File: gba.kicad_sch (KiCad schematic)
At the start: 16 parts, among them IC1 STM32MP157AAB3, IC7 S40FC004C1B2C00000, SW1 SW_MEC_5G, SW2 SW_MEC_5G

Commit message: added some part footprints
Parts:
- C1, C2: footprint (none) -> Capacitor_SMD:C_0603_1608Metric; MFN (none) -> 77-VJ0603Y103MXAPBC
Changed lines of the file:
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@@
       (effects (font (size 1.27 1.27)) (justify left))
     )
-    (property "Footprint" "" (at 232.41 40.64 0)
+    (property "Footprint" "Capacitor_SMD:C_0603_1608Metric" (at 232.41 40.64 0)
       (effects (font (size 1.27 1.27)) hide)
     )
@@
       (effects (font (size 1.27 1.27)) hide)
     )
-    (property "MFN" "" (at 232.41 40.64 0)
+    (property "MFN" " 77-VJ0603Y103MXAPBC " (at 232.41 40.64 0)
       (effects (font (size 1.27 1.27)) hide)
     )
@@
       (effects (font (size 1.27 1.27)) (justify left))
     )
-    (property "Footprint" "" (at 256.54 40.64 0)
+    (property "Footprint" "Capacitor_SMD:C_0603_1608Metric" (at 256.54 40.64 0)
       (effects (font (size 1.27 1.27)) hide)
     )
@@
       (effects (font (size 1.27 1.27)) hide)
     )
-    (property "MFN" "" (at 256.54 40.64 0)
+    (property "MFN" " 77-VJ0603Y103MXAPBC " (at 256.54 40.64 0)
       (effects (font (size 1.27 1.27)) hide)
     )

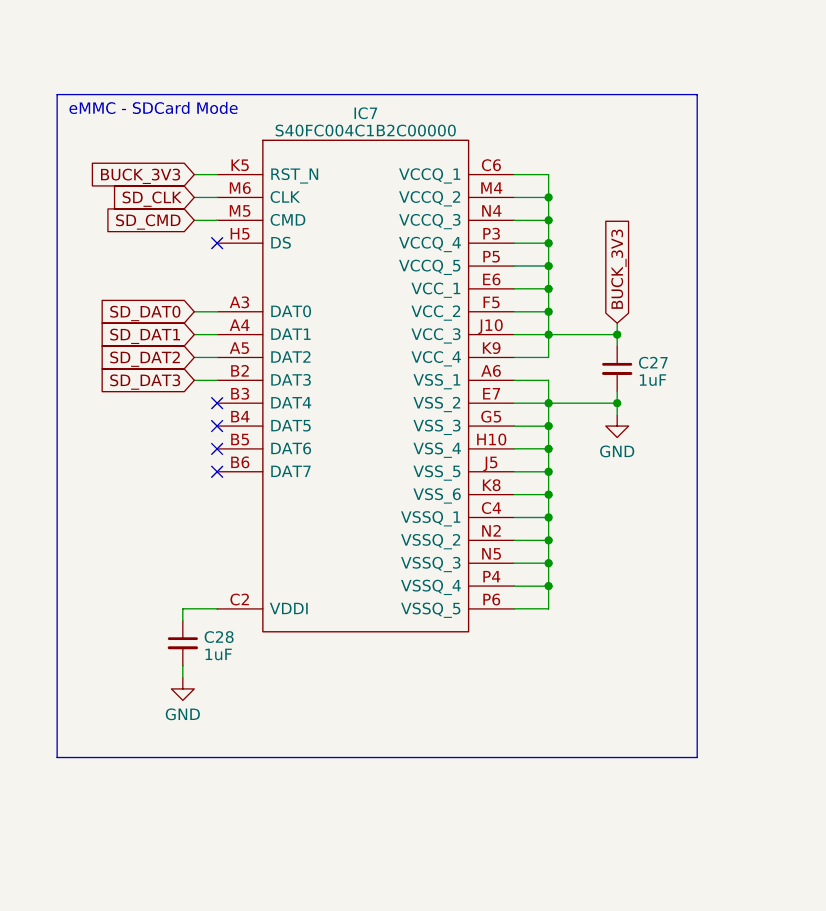
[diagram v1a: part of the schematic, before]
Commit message: Add Labels for DDR & DDR Power
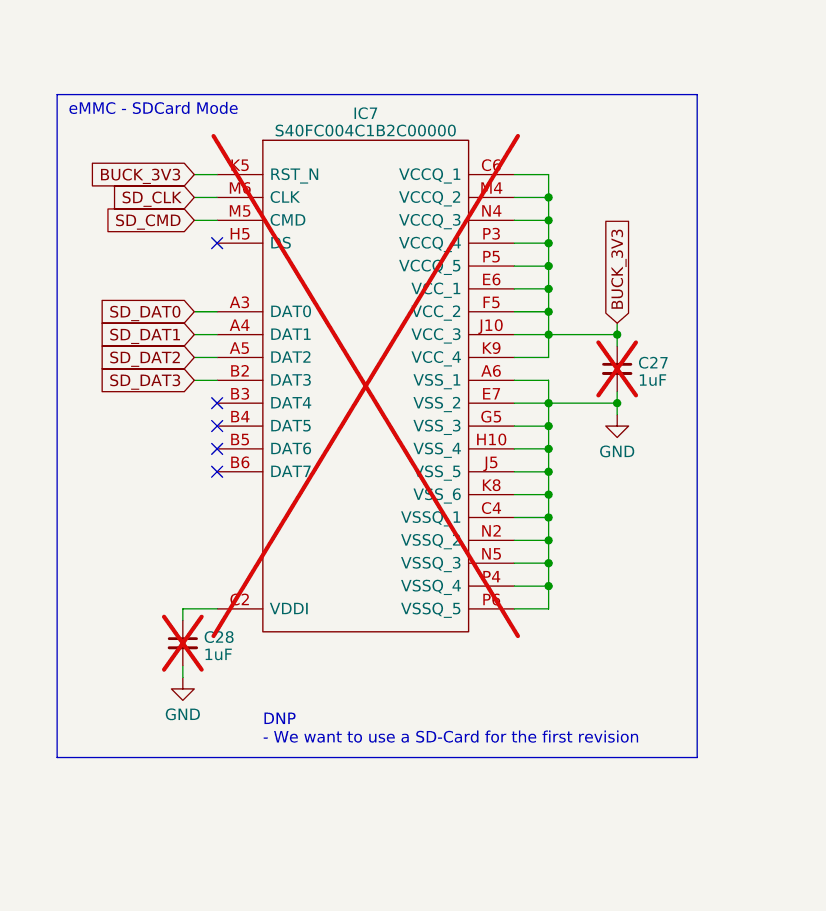
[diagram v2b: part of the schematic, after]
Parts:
- C27, C28, IC7: now not fitted
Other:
- note added: "DNP - We want to use a SD-Card for the first revision"
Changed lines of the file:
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@@
+    (effects (font (size 1.27 1.27)) (justify left bottom))
+  )
+  (text "DNP\n- We want to use a SD-Card for the first revision"
+    (at 353.06 97.79 0)
     (effects (font (size 1.27 1.27)) (justify left bottom))
   )
@@
   )
   (symbol (lib_id "Device:C_Small") (at 344.17 86.36 0) (unit 1)
-    (in_bom yes) (on_board yes) (dnp no) (fields_autoplaced)
+    (in_bom yes) (on_board yes) (dnp yes) (fields_autoplaced)
     (property "Reference" "C28" (at 346.4941 85.7226 0)
       (effects (font (size 1.27 1.27)) (justify left))
@@
   )
   (symbol (lib_id "Device:C_Small") (at 392.43 55.88 0) (unit 1)
-    (in_bom yes) (on_board yes) (dnp no) (fields_autoplaced)
+    (in_bom yes) (on_board yes) (dnp yes) (fields_autoplaced)
     (property "Reference" "C27" (at 394.7541 55.2426 0)
       (effects (font (size 1.27 1.27)) (justify left))
@@
   )
   (symbol (lib_id "ARMband:S40FC004C1B2C00000") (at 384.81 34.29 0) (unit 1)
-    (in_bom yes) (on_board yes) (dnp no) (fields_autoplaced)
+    (in_bom yes) (on_board yes) (dnp yes) (fields_autoplaced)
     (property "Reference" "IC7" (at 364.49 27.5209 0)
       (effects (font (size 1.27 1.27)))

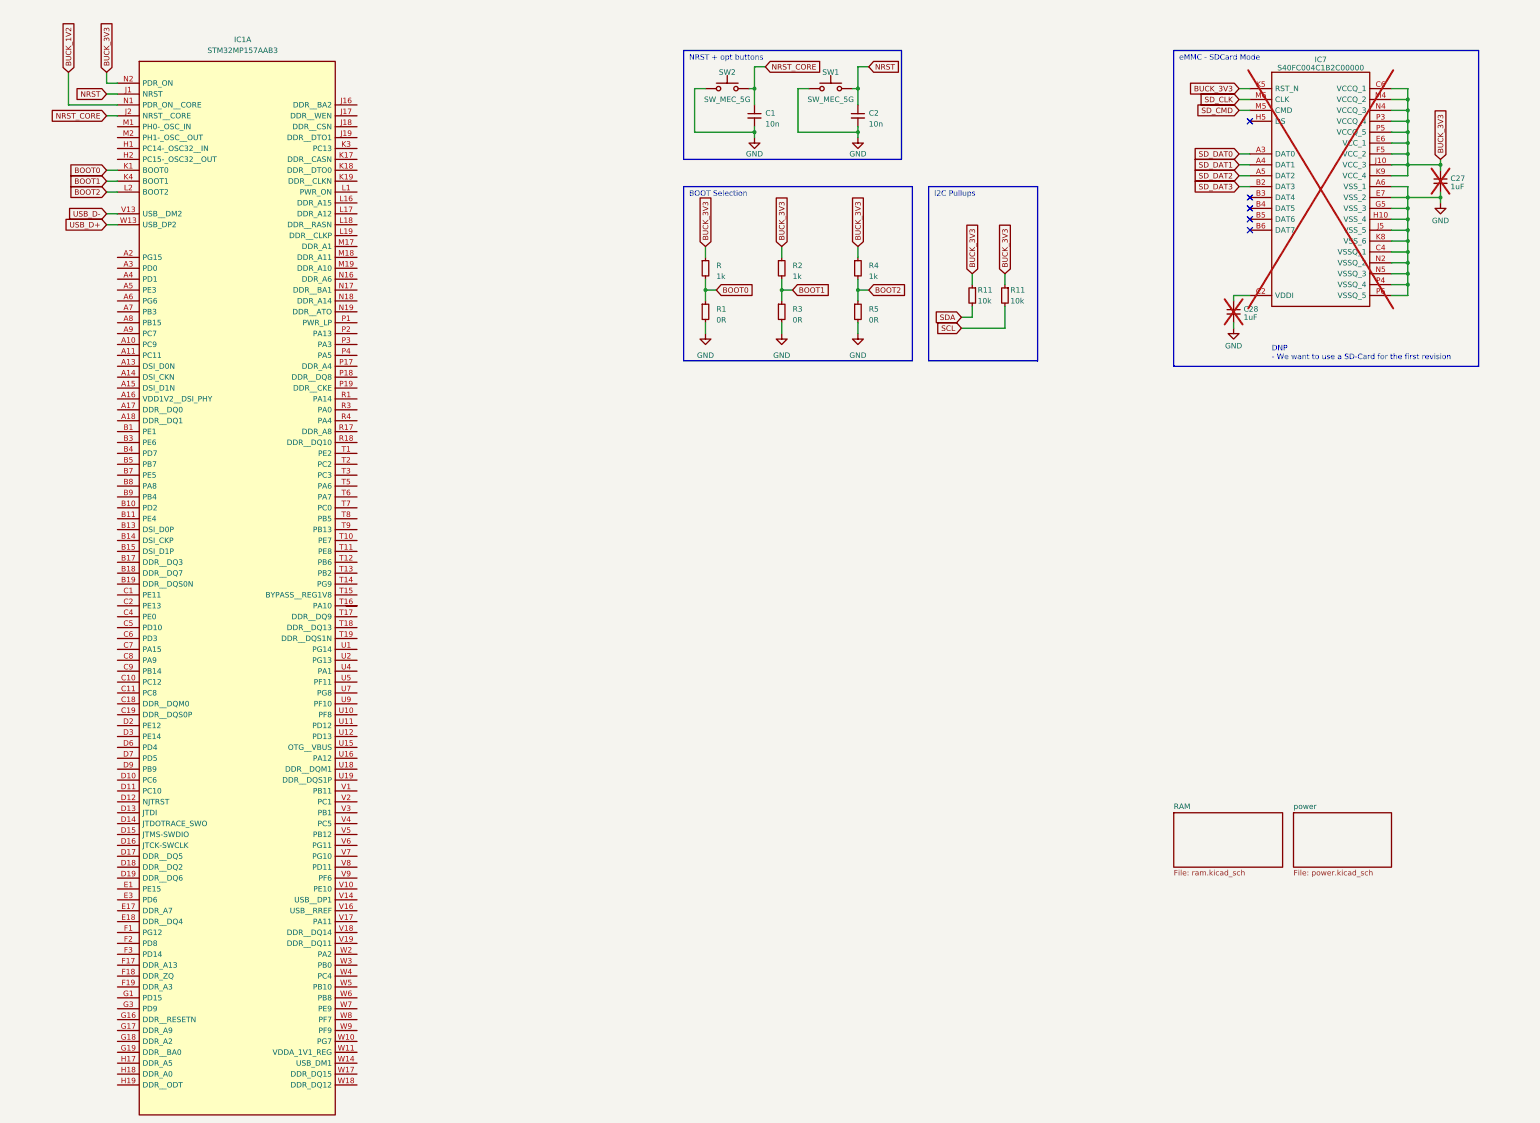
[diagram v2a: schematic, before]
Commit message: Add DDR routing to STM32MP1
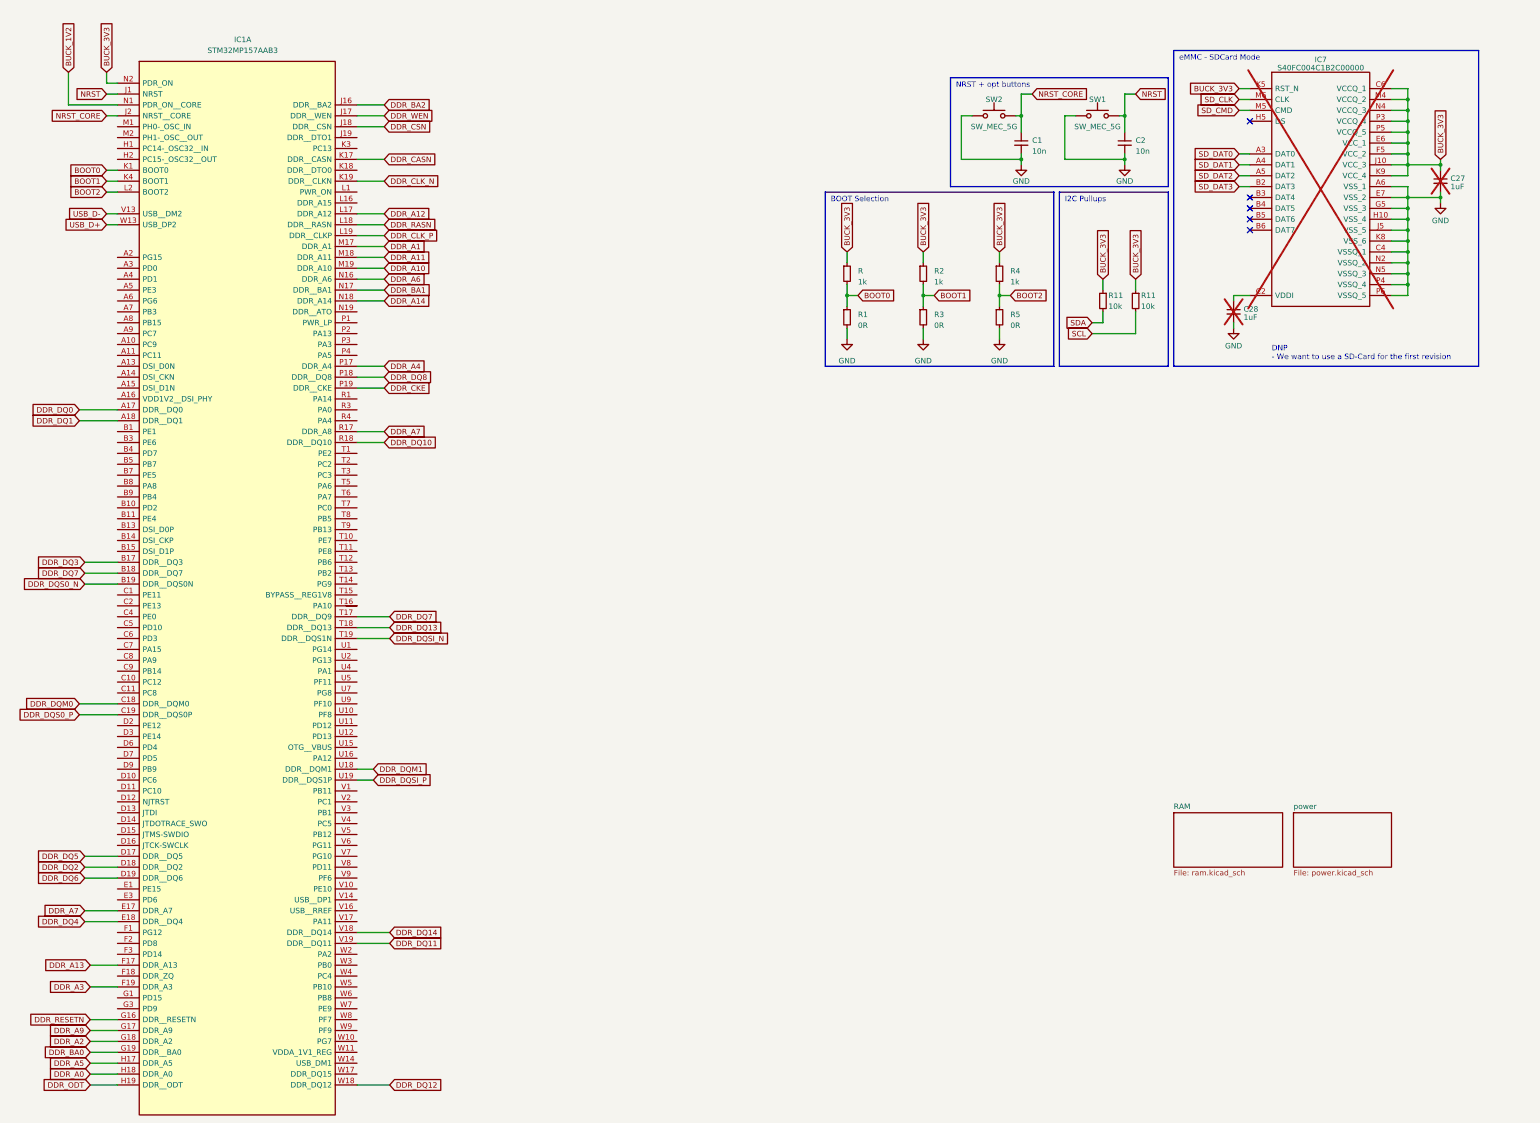
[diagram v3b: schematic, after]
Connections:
- net DDR_DQ0: now reaches IC1.A17 (DDR__DQ0)
- net DDR_DQ1: now reaches IC1.A18 (DDR__DQ1)
- net DDR_DQ3: now reaches IC1.B17 (DDR__DQ3)
- net DDR_DQ7: now reaches IC1.B18 (DDR__DQ7)
- net DDR_DQ7: now also IC1.T17 (DDR__DQ9)
- net DDR_DQS0_N: now reaches IC1.B19 (DDR__DQS0N)
- net DDR_DQM0: now reaches IC1.C18 (DDR__DQM0)
- net DDR_DQS0_P: now reaches IC1.C19 (DDR__DQS0P)
- net DDR_DQ5: now reaches IC1.D17 (DDR__DQ5)
- net DDR_DQ2: now reaches IC1.D18 (DDR__DQ2)
- net DDR_DQ6: now reaches IC1.D19 (DDR__DQ6)
- net DDR_A7: now reaches IC1.E17 (DDR_A7)
- net DDR_A7: now also IC1.R17 (DDR_A8)
- net DDR_DQ4: now reaches IC1.E18 (DDR__DQ4)
- net DDR_A13: now reaches IC1.F17 (DDR_A13)
- net DDR_A3: now reaches IC1.F19 (DDR_A3)
- net DDR_RESETN: now reaches IC1.G16 (DDR__RESETN)
- net DDR_A9: now reaches IC1.G17 (DDR_A9)
- net DDR_A2: now reaches IC1.G18 (DDR_A2)
- net DDR_BA0: now reaches IC1.G19 (DDR__BA0)
- net DDR_A5: now reaches IC1.H17 (DDR_A5)
- net DDR_A0: now reaches IC1.H18 (DDR_A0)
- net DDR_ODT: now reaches IC1.H19 (DDR__ODT)
- net DDR_BA2: now reaches IC1.J16 (DDR__BA2)
- net DDR_WEN: now reaches IC1.J17 (DDR__WEN)
- net DDR_CSN: now reaches IC1.J18 (DDR__CSN)
- net DDR_CASN: now reaches IC1.K17 (DDR__CASN)
- net DDR_CLK_N: now reaches IC1.K19 (DDR__CLKN)
- net DDR_A12: now reaches IC1.L17 (DDR_A12)
- net DDR_RASN: now reaches IC1.L18 (DDR__RASN)
- net DDR_CLK_P: now reaches IC1.L19 (DDR__CLKP)
- net DDR_A1: now reaches IC1.M17 (DDR_A1)
- net DDR_A11: now reaches IC1.M18 (DDR_A11)
- net DDR_A10: now reaches IC1.M19 (DDR_A10)
- net DDR_A6: now reaches IC1.N16 (DDR_A6)
- net DDR_BA1: now reaches IC1.N17 (DDR__BA1)
- net DDR_A14: now reaches IC1.N18 (DDR_A14)
- net DDR_A4: now reaches IC1.P17 (DDR_A4)
- net DDR_DQ8: now reaches IC1.P18 (DDR__DQ8)
- net DDR_CKE: now reaches IC1.P19 (DDR__CKE)
- net DDR_DQ10: now reaches IC1.R18 (DDR__DQ10)
- net DDR_DQ13: now reaches IC1.T18 (DDR__DQ13)
- net DDR_DQSI_N: now reaches IC1.T19 (DDR__DQS1N)
- net DDR_DQM1: now reaches IC1.U18 (DDR__DQM1)
- net DDR_DQSI_P: now reaches IC1.U19 (DDR__DQS1P)
- net DDR_DQ14: now reaches IC1.V18 (DDR__DQ14)
- net DDR_DQ11: now reaches IC1.V19 (DDR__DQ11)
- net DDR_DQ12: now reaches IC1.W18 (DDR_DQ12)
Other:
- moved on the sheet: C1, C2, R, R1, R11, R2, R3, R4, R5, SW1, SW2
